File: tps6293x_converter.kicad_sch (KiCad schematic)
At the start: 11 parts, among them U1 TPS62933

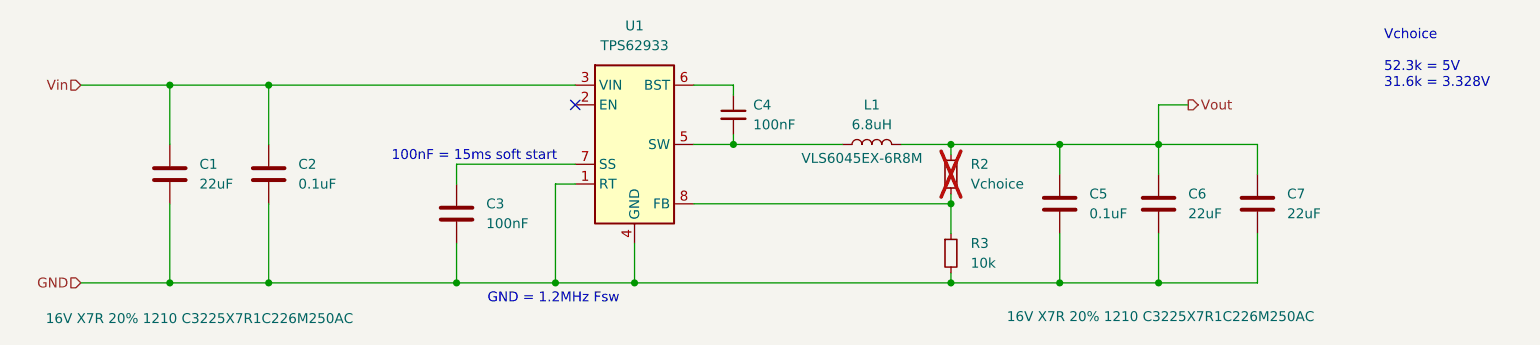
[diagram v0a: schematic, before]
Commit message: pcb: first placement
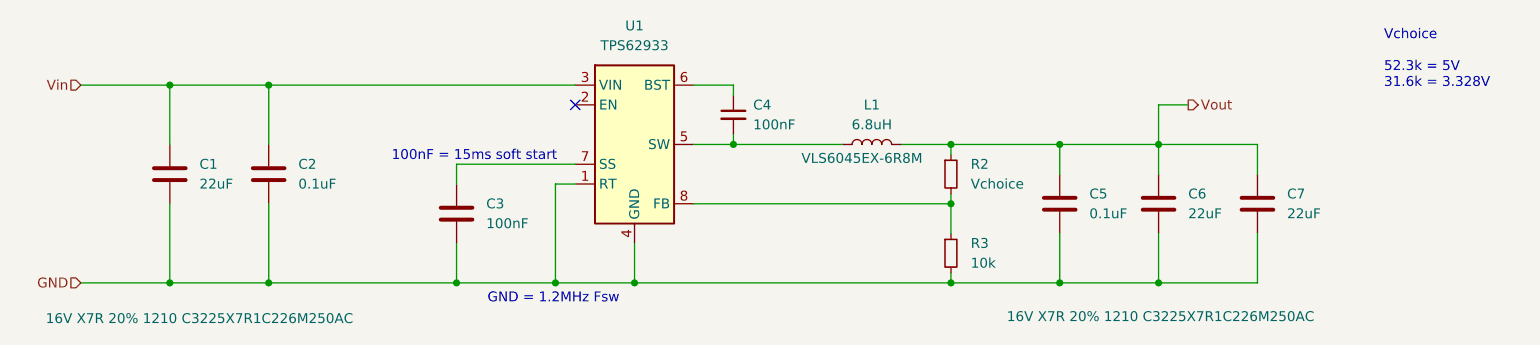
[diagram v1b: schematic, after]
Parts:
- R2: footprint SMD:0603_1608Metric_DNI_NoPaste -> Resistor_SMD:R_0603_1608Metric; now fitted
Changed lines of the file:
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@@
 		(in_bom yes)
 		(on_board yes)
-		(dnp yes)
+		(dnp no)
 		(fields_autoplaced yes)
 		(property "Reference" "R2"
@@
 			)
 		)
-		(property "Footprint" "SMD:0603_1608Metric_DNI_NoPaste"
+		(property "Footprint" "Resistor_SMD:R_0603_1608Metric"
 			(at 137.16 36.83 0)
 			(effects

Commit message: pcb: couple little changes
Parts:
- R2: value Vchoice -> 52.3k
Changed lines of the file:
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@@
 			)
 		)
-		(property "Value" "Vchoice"
+		(property "Value" "52.3k"
 			(at 139.7 38.0999 0)
 			(effects
